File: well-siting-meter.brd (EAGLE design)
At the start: 104.3 x 76.4 mm, 46 parts, among them J2 7805, T1 MOSFET-NCHANNELFQP30N06L, U1 LCD-16X2NOHOLES, U2 ARDUINO_PRO_MINI, U3 EC2, U4 EC2, U5 AD623, U6 AD623

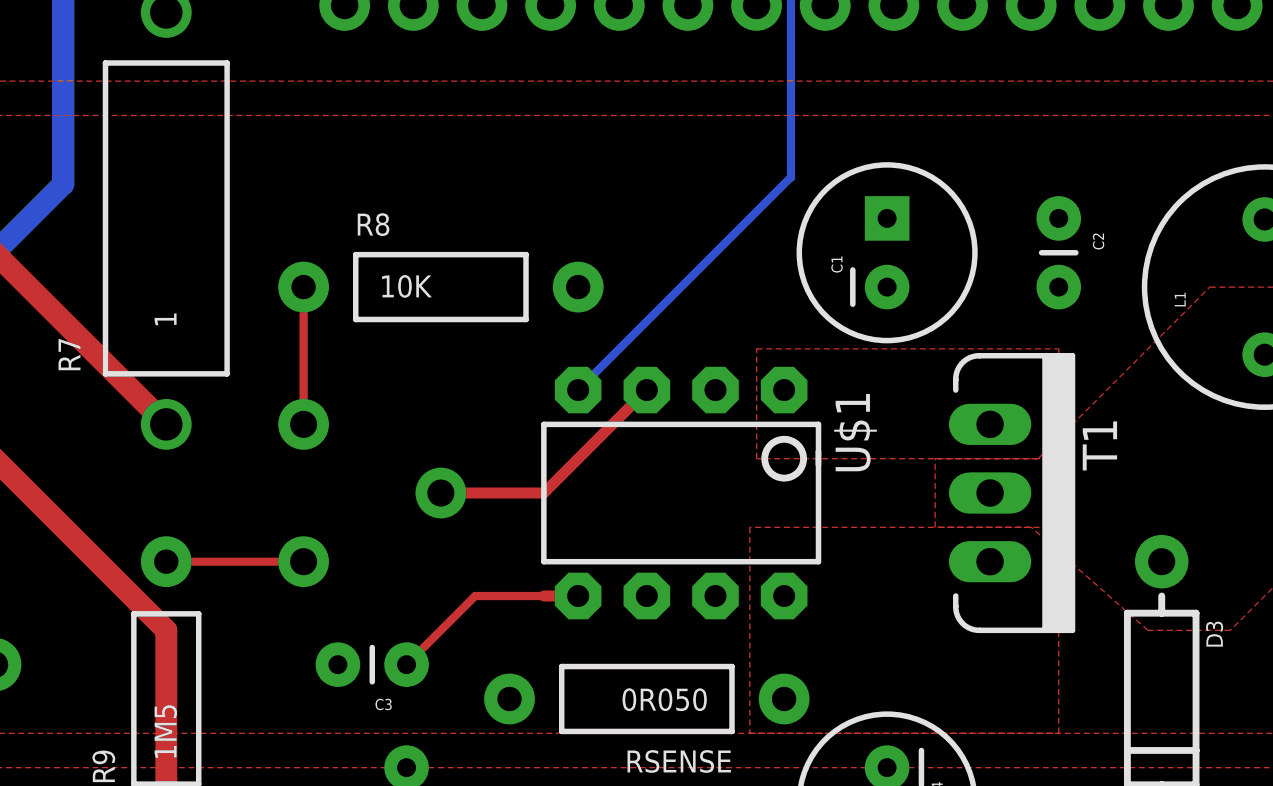
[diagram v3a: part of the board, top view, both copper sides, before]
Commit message: adding part numbers
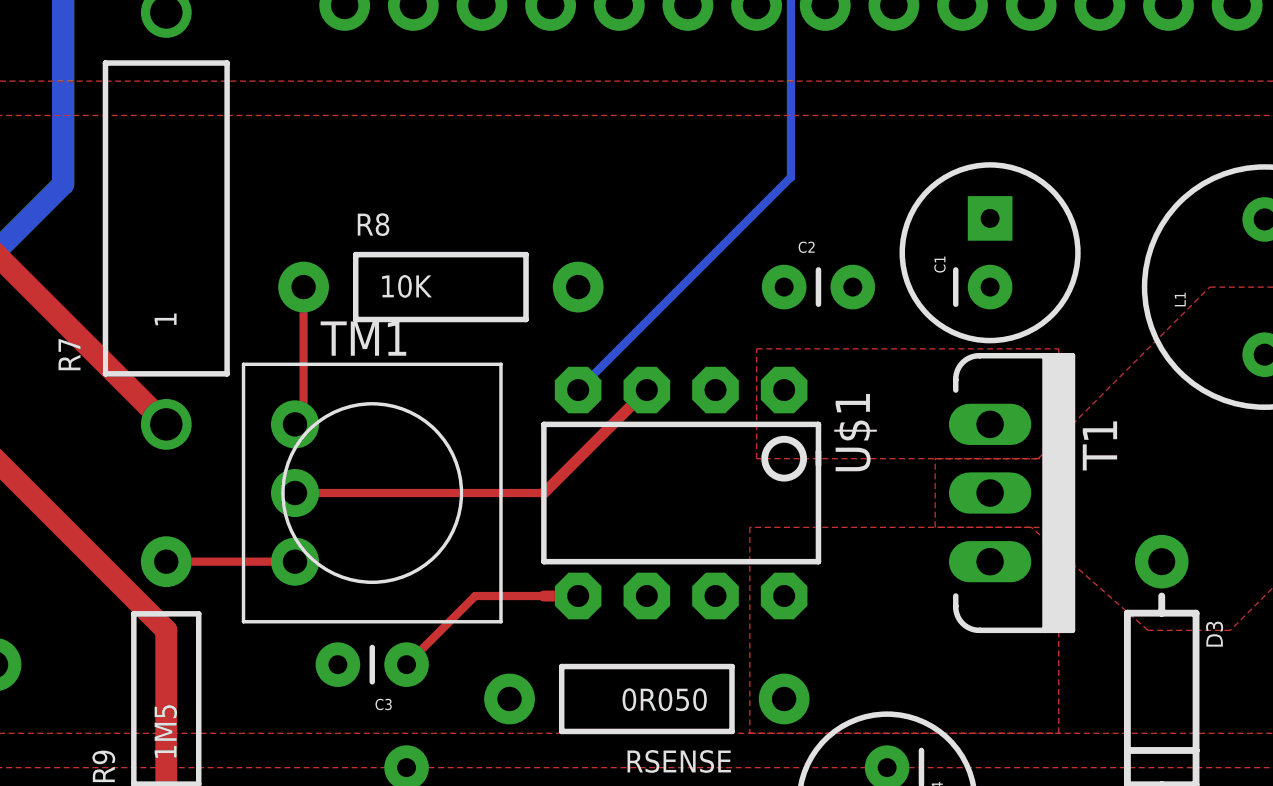
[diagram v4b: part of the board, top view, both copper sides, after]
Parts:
- removed VR1: 5K, SparkFun-Electromechanical:TRIM_POT
- added TM1: (no value), adafruit:TRIM-3386
- moved C2 10.5 mm to (58.4, 24.1), turned to 0 degrees
- moved C1 3.81 mm to (66.0, 25.4)
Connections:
- net N$15: now also TM1.2; no longer VR1.1
- net N$6: now also TM1.3; no longer VR1.3
- net N$8: now also TM1.1; no longer VR1.2
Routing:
- net N$15: track 9.20 -> 14.6 mm
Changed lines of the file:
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@@
 <layer number="230" name="230bmp" color="7" fill="1" visible="yes" active="yes"/>
 <layer number="231" name="231bmp" color="7" fill="1" visible="yes" active="yes"/>
+<layer number="232" name="Eagle3D_PG2" color="7" fill="1" visible="no" active="no"/>
+<layer number="233" name="Eagle3D_PG3" color="7" fill="1" visible="no" active="no"/>
 <layer number="248" name="Housing" color="7" fill="1" visible="yes" active="yes"/>
 <layer number="249" name="Edge" color="7" fill="1" visible="yes" active="yes"/>
@@
 </autorouter>
 <elements>
-<element name="U3" library="ec2" package="EC2" value="EC2" x="24.13" y="21.59" rot="R180"/>
-<element name="U4" library="ec2" package="EC2" value="EC2" x="10.16" y="21.59" rot="R180"/>
-<element name="U2" library="SparkFun-Boards" package="ARDUINO_PRO_MINI" value="ARDUINO_PRO_MINI" x="59.69" y="48.26" rot="R270"/>
-<element name="U5" library="ad623" package="AD623" value="AD623" x="24.13" y="45.72" rot="R180"/>
-<element name="U6" library="ad623" package="AD623" value="AD623" x="10.16" y="45.72" rot="R180"/>
+<element name="U3" library="ec2" package="EC2" value="EC2" x="24.13" y="21.59" rot="R180">
+<attribute name="PN" value="399-11029-5-ND" x="24.13" y="21.59" size="1.778" layer="27" rot="R180" display="off"/>
+</element>
+<element name="U4" library="ec2" package="EC2" value="EC2" x="10.16" y="21.59" rot="R180">
+<attribute name="PN" value="399-11029-5-ND" x="10.16" y="21.59" size="1.778" layer="27" rot="R180" display="off"/>
+</element>
+<element name="U2" library="SparkFun-Boards" package="ARDUINO_PRO_MINI" value="ARDUINO_PRO_MINI" x="59.69" y="48.26" rot="R270">
+<attribute name="PN" value="1568-1055-ND" x="59.69" y="48.26" size="1.778" layer="27" rot="R270" display="off"/>
+</element>
+<element name="U5" library="ad623" package="AD623" value="AD623" x="24.13" y="45.72" rot="R180">
+<attribute name="PN" value="AD623ANZ-ND" x="24.13" y="45.72" size="1.778" layer="27" rot="R180" display="off"/>
+</element>
+<element name="U6" library="ad623" package="AD623" value="AD623" x="10.16" y="45.72" rot="R180">
+<attribute name="PN" value="AD623ANZ-ND" x="10.16" y="45.72" size="1.778" layer="27" rot="R180" display="off"/>
+</element>
 <element name="Q1" library="SparkFun-DiscreteSemi" package="TO-92" value="" x="24.13" y="6.35" rot="R180">
 <attribute name="PROD_ID" value="TRANS-09536" x="24.13" y="6.35" size="1.778" layer="27" rot="R180" display="off"/>
@@
 <attribute name="PN" value="490-7202-1-ND" x="89.408" y="38.608" size="1.778" layer="27" rot="R90" display="off"/>
 </element>
-<element name="U1" library="SparkFun-Displays" package="LCD-16X2_NOHOLES" value="LCD-16X2NOHOLES" x="48.26" y="19.05" rot="MR0"/>
+<element name="U1" library="SparkFun-Displays" package="LCD-16X2_NOHOLES" value="LCD-16X2NOHOLES" x="48.26" y="19.05" rot="MR0">
+<attribute name="PN" value="1528-1502-ND" x="48.26" y="19.05" size="1.778" layer="28" rot="MR0" display="off"/>
+</element>
 <element name="J12" library="SparkFun-Connectors" package="BANANA_CONN" value="" x="7.62" y="62.23"/>
 <element name="J7" library="SparkFun-Connectors" package="BANANA_CONN" value="" x="88.9" y="62.23"/>
@@
 </element>
 <element name="L1" library="SparkFun-Passives" package="RLB0912" value="" x="76.2" y="24.13" rot="R90"/>
-<element name="C1" library="SparkFun-Passives" package="CPOL-RADIAL-100UF-25V" value="" x="62.23" y="25.4" rot="R90"/>
-<element name="C2" library="SparkFun-Passives" package="CAP-PTH-SMALL" value="" x="68.58" y="26.67" rot="R270"/>
+<element name="C1" library="SparkFun-Passives" package="CPOL-RADIAL-100UF-25V" value="" x="66.04" y="25.4" rot="R90"/>
+<element name="C2" library="SparkFun-Passives" package="CAP-PTH-SMALL" value="" x="58.42" y="24.13"/>
 <element name="C3" library="SparkFun-Passives" package="CAP-PTH-SMALL" value="" x="44.45" y="10.16" rot="R180"/>
 <element name="T1" library="SparkFun-DiscreteSemi" package="TO220V" value="MOSFET-NCHANNELFQP30N06L" x="66.04" y="16.51" rot="R270">
 <attribute name="PROD_ID" value="TRANS-10060" x="66.04" y="16.51" size="1.778" layer="27" rot="R270" display="off"/>
-</element>
-<element name="D3" library="SparkFun-DiscreteSemi" package="DIODE-1N4001" value="" x="72.39" y="8.89" rot="R270"/>
+<attribute name="PN" value="FDP33N25-ND" x="66.04" y="16.51" size="1.778" layer="27" rot="R270" display="off"/>
+</element>
+<element name="D3" library="SparkFun-DiscreteSemi" package="DIODE-1N4001" value="" x="72.39" y="8.89" rot="R270">
+<attribute name="PN" value="EGP20FCT-ND" x="72.39" y="8.89" size="1.778" layer="27" rot="R270" display="off"/>
+</element>
 <element name="RSENSE" library="SparkFun-Passives" package="AXIAL-0.4" value="0R050" x="53.34" y="8.89" rot="R180"/>
-<element name="VR1" library="SparkFun-Electromechanical" package="TRIM_POT" value="5K" x="40.64" y="16.51"/>
 <element name="R8" library="SparkFun-Passives" package="AXIAL-0.4" value="10K" x="45.72" y="24.13"/>
 <element name="R9" library="SparkFun-Passives" package="AXIAL-0.4" value="1M5" x="35.56" y="8.89" rot="R90"/>
 <element name="C6" library="SparkFun-Passives" package="CAP-PTH-SMALL" value="" x="44.45" y="3.81" rot="R90"/>
 <element name="C4" library="SparkFun-Passives" package="CPOL-RADIAL-100UF-25V" value="" x="62.23" y="5.08" rot="R270"/>
-<element name="U$1" library="max1771" package="DIP-08" value="MAX1771" x="54.61" y="16.51" rot="R180"/>
+<element name="U$1" library="max1771" package="DIP-08" value="MAX1771" x="54.61" y="16.51" rot="R180">
+<attribute name="PN" value="MAX1771CPA+-ND" x="54.61" y="16.51" size="1.778" layer="27" rot="R180" display="off"/>
+</element>
 <element name="R10" library="SparkFun-Passives" package="AXIAL-0.4" value="1.02K" x="40.64" y="50.8" rot="R270"/>
 <element name="R11" library="SparkFun-Passives" package="AXIAL-0.4" value="1.02K" x="35.56" y="50.8" rot="R270"/>
 <element name="C10" library="SparkFun-Passives" package="CAP-PTH-SMALL" value="" x="35.56" y="40.64" rot="R270"/>
 <element name="C9" library="SparkFun-Passives" package="CAP-PTH-SMALL" value="" x="40.64" y="40.64" rot="R270"/>
+<element name="TM1" library="adafruit" package="TRIM-3386" value="" x="43.18" y="16.51" rot="R270"/>
 </elements>
 <signals>
@@
 <signal name="N$6">
 <contactref element="R9" pad="P$2"/>
-<contactref element="VR1" pad="3"/>
-<wire x1="35.56" y1="13.97" x2="40.64" y2="13.97" width="0.3048" layer="1"/>
+<contactref element="TM1" pad="3"/>
+<wire x1="35.56" y1="13.97" x2="40.3225" y2="13.97" width="0.3048" layer="1"/>
 </signal>
 <signal name="N$8">
-<contactref element="VR1" pad="2"/>
 <contactref element="R8" pad="P$1"/>
-<wire x1="40.64" y1="24.13" x2="40.64" y2="19.05" width="0.3048" layer="1"/>
+<contactref element="TM1" pad="1"/>
+<wire x1="40.64" y1="24.13" x2="40.64" y2="19.3675" width="0.3048" layer="1"/>
+<wire x1="40.64" y1="19.3675" x2="40.3225" y2="19.05" width="0.3048" layer="1"/>
 </signal>
 <signal name="N$15">
-<contactref element="VR1" pad="1"/>
 <contactref element="U$1" pad="3"/>
-<wire x1="45.72" y1="16.51" x2="49.53" y2="16.51" width="0.4064" layer="1"/>
 <wire x1="49.53" y1="16.51" x2="53.34" y2="20.32" width="0.4064" layer="1"/>
+<contactref element="TM1" pad="2"/>
+<wire x1="40.3225" y1="16.51" x2="49.53" y2="16.51" width="0.3048" layer="1"/>
 </signal>
 <signal name="SHDN">
